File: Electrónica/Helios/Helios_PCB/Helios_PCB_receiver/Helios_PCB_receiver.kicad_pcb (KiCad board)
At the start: 2 copper layers, 34 x 29.5 mm, 11 parts, among them J0 Connector, U0 OPA2380, U1 OPA2380

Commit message: Helios: Receiver V1.3
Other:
- board text added: "0 3 G"
- board text added: "2 1 V"
- board text added: "G 3 0"
- board text added: "Helios V1.3 2022"
- board text added: "J.B.A."
- board text added: "Rcv."
- board text added: "V 1 2"
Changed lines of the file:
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@@
     (property "Sheetname" "")
     (attr through_hole)
-    (fp_text reference "J0" (at 1.27 -2.33 90) (layer "F.SilkS")
+    (fp_text reference "J0" (at 1.27 -2.33 90) (layer "F.SilkS") hide
       (effects (font (size 1 1) (thickness 0.15)))
     )
@@
       (net 3 "Net-(F1-Pad1)") (pintype "passive"))
   )
+  (gr_line (start 169.2 100) (end 173.3 100) (layer "B.SilkS") (width 0.15))
+  (gr_line (start 172 102) (end 172 98.1) (layer "B.SilkS") (width 0.15))
+  (gr_line (start 170.3 98.1) (end 170.3 102) (layer "B.SilkS") (width 0.15))
+  (gr_line (start 170.3 98.1) (end 170.3 102) (layer "F.SilkS") (width 0.15))
+  (gr_line (start 169.2 100) (end 173.3 100) (layer "F.SilkS") (width 0.15))
+  (gr_line (start 172 98.1) (end 172 102) (layer "F.SilkS") (width 0.15))
   (gr_circle (center 165 100) (end 175 100) (layer "Dwgs.User") (width 0.15) (fill none))
   (gr_line (start 165 100) (end 152.5 87.5) (layer "Dwgs.User") (width 0.15))
@@
   (gr_line (start 174.5 103) (end 155.450535 103.01562) (layer "Edge.Cuts") (width 0.1))
   (gr_arc (start 173.48684 85.270692) (mid 181.999381 100) (end 173.48684 114.729308) (layer "Edge.Cuts") (width 0.15))
+  (gr_text "2 1 V" (at 171.25 101.4) (layer "B.SilkS")
+    (effects (font (size 1 1) (thickness 0.15)) (justify mirror))
+  )
+  (gr_text "G 3 0" (at 171.25 98.75) (layer "B.SilkS")
+    (effects (font (size 1 1) (thickness 0.15)) (justify mirror))
+  )
+  (gr_text "Helios\nV1.3\n2022\n" (at 160.5 100) (layer "B.SilkS")
+    (effects (font (size 1 1) (thickness 0.15)) (justify left mirror))
+  )
+  (gr_text "V 1 2" (at 171.3 101.4) (layer "F.SilkS")
+    (effects (font (size 1 1) (thickness 0.15)))
+  )
+  (gr_text "J.B.A." (at 158.7 100.7) (layer "F.SilkS")
+    (effects (font (size 1 1) (thickness 0.15)))
+  )
+  (gr_text "Rcv." (at 159.2 99.2) (layer "F.SilkS")
+    (effects (font (size 1 1) (thickness 0.15)))
+  )
+  (gr_text "0 3 G" (at 171.2 98.8) (layer "F.SilkS")
+    (effects (font (size 1 1) (thickness 0.15)))
+  )
   (segment (start 152.05 96.05) (end 152.05 94.25) (width 0.25) (layer "F.Cu") (net 1))
   (segment (start 152.325 96.325) (end 152.05 96.05) (width 0.25) (layer "F.Cu") (net 1))

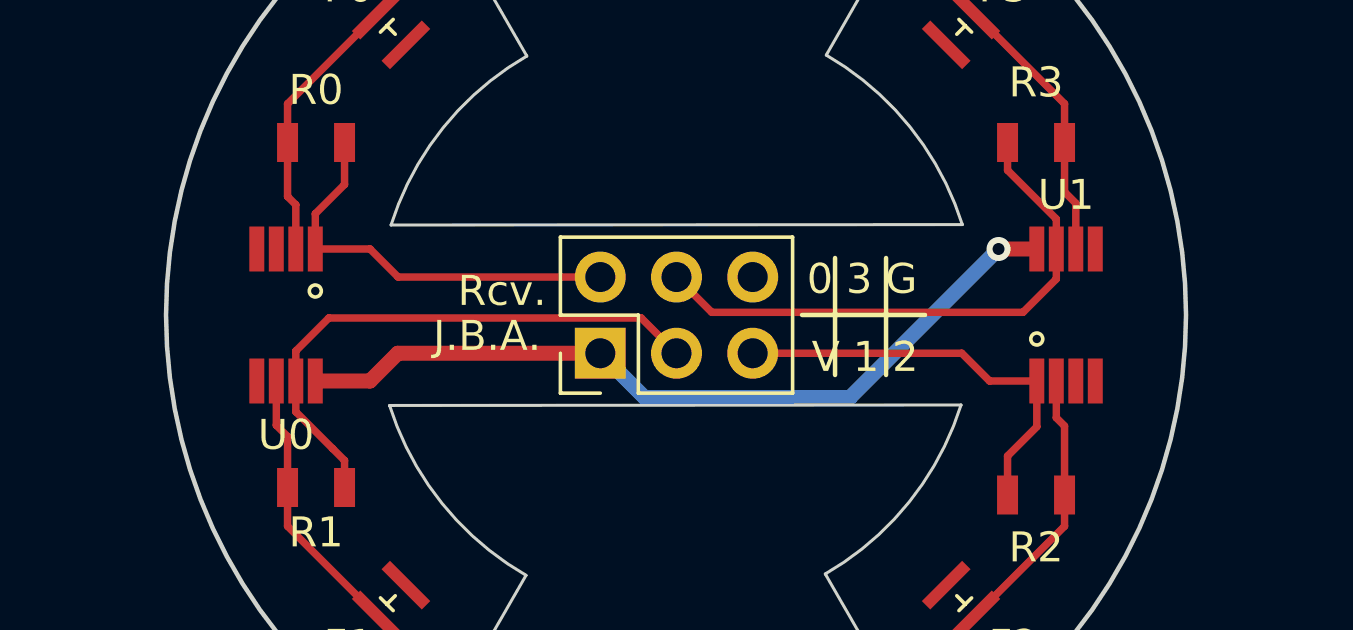
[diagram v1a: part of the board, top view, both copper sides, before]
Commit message: Helios: Updated Silkscreen
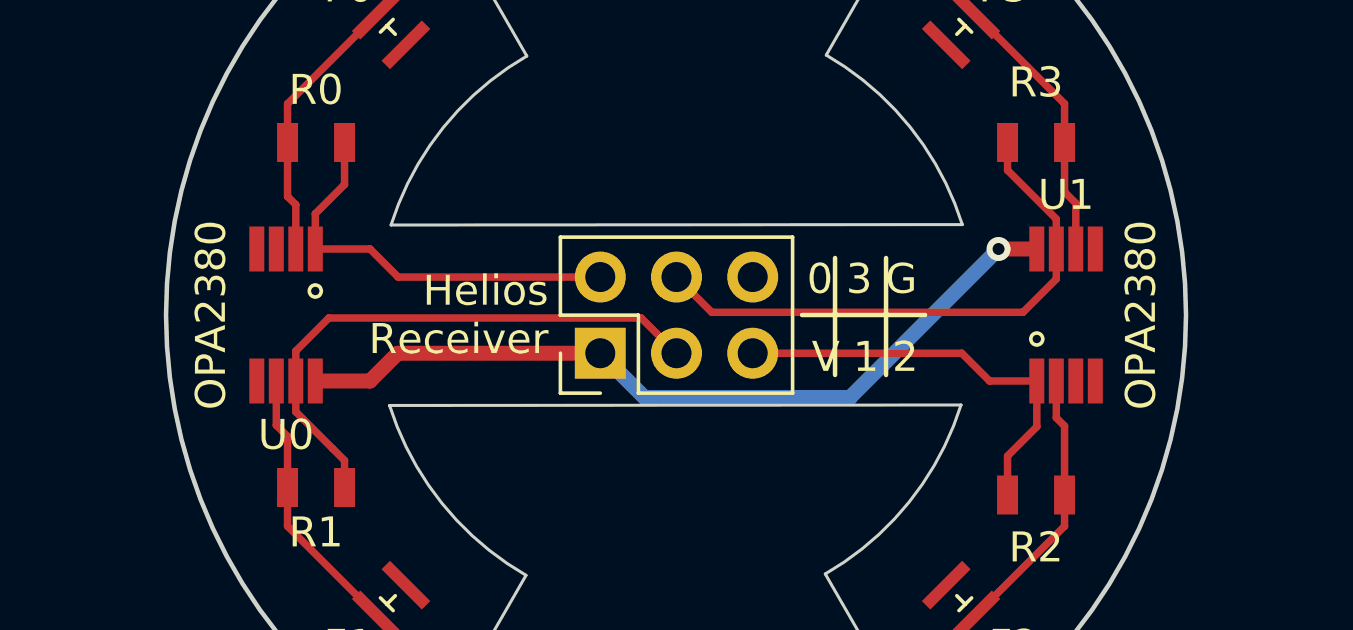
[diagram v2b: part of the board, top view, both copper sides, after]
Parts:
- added G***: LOGO, LOGO, B.Cu at (150.0, 100.0)
- added G***: LOGO, LOGO, B.Cu at (177.5, 94.2)
- added G***: LOGO, LOGO, B.Cu at (178.2, 99.8)
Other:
- board text added: "Helios Receiver"
- board text added: "JaimeBravoAlgaba Helios_SoftRobot"
- board text added: "Rpd"
- board text removed: "J.B.A."
- board text removed: "Rcv."

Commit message: Last changes V1.3
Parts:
- removed the G*** at (177.5, 94.2)
- removed the G*** at (178.2, 99.8)
- added G***: LOGO, LOGO, B.Cu at (174.7, 107.6)
- added G***: LOGO, LOGO, B.Cu at (178.1, 99.9)
- added G***: LOGO, LOGO, B.Cu at (177.7, 94.4)
- added G***: LOGO, LOGO, B.Cu at (174.5, 90.5)
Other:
- board text added: "5V"
- board text added: "AE RESET"
- board text added: "Colabora:"
- board text added: "RCV"
- board text removed: "Helios Receiver"
